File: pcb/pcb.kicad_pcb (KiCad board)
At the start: 2 copper layers, 70 x 21 mm, 20 parts, among them J1 BAT+, J2 BAT-, J3 Molex, SW1 Reset, SW2 Flash, U1 CP2102, U2 ESP-12F, U3 TP4056, U4 GY-521, U5 VREG

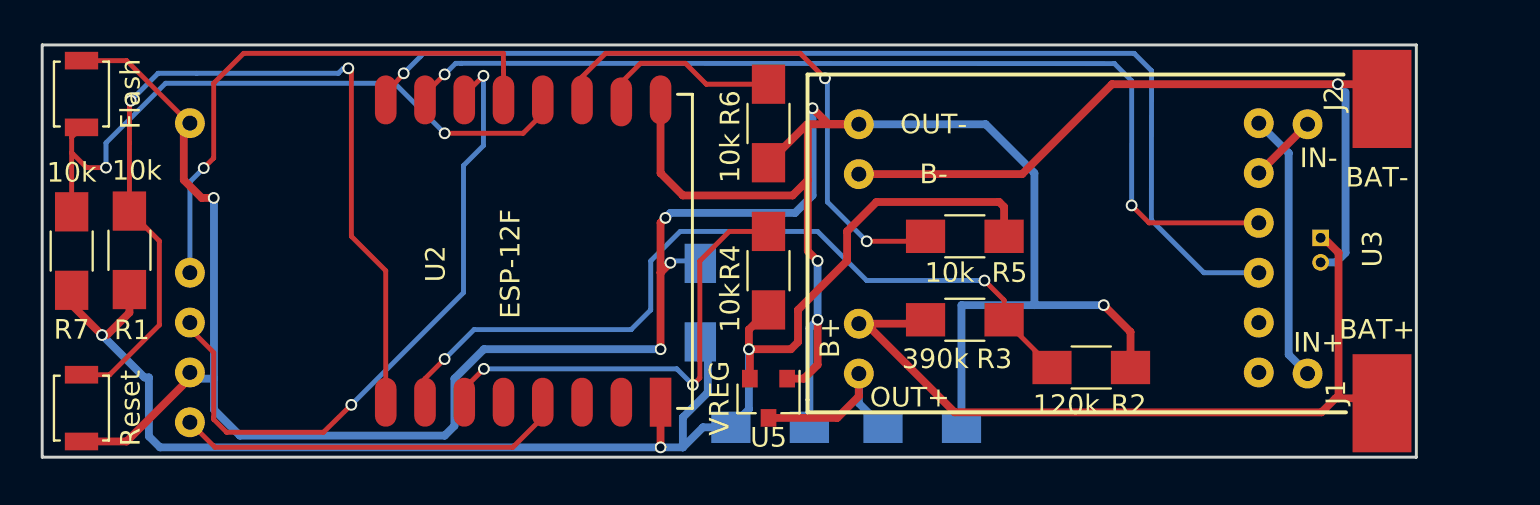
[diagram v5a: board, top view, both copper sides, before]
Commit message: Ignore BOM, remove old BOM, non-right-angle a few more traces
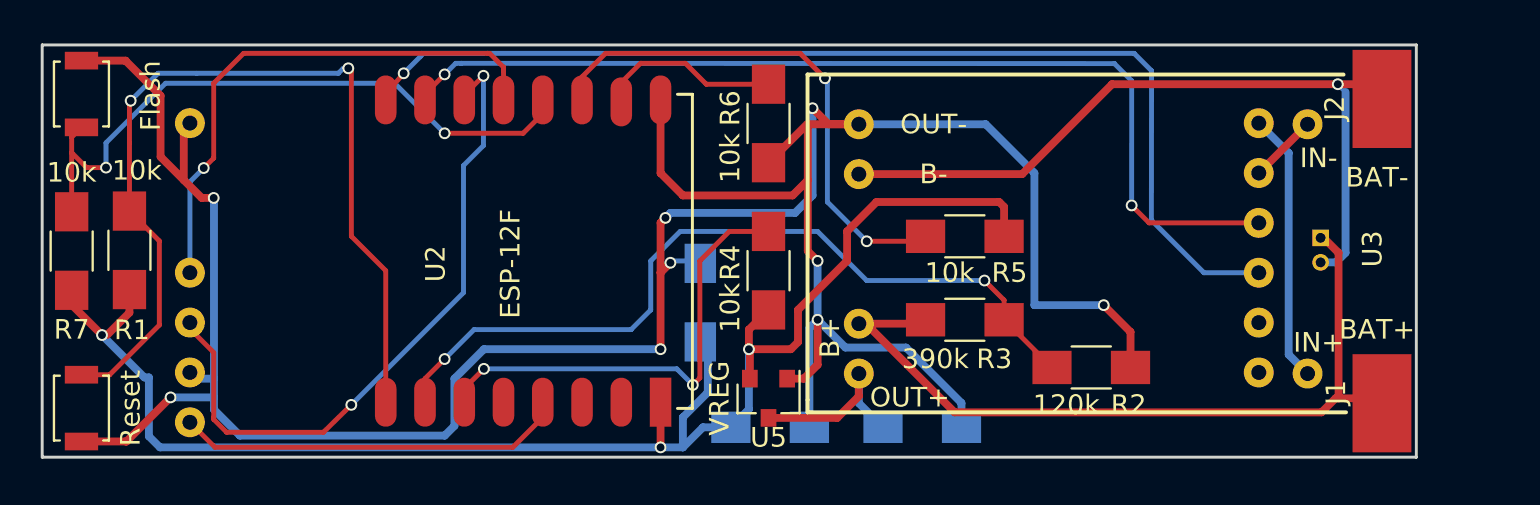
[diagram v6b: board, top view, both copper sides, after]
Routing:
- net /GND: track 152.5 -> 156.5 mm, vias 8 -> 9
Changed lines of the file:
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@@
     (area 106.162599 87.634999 176.312601 108.785001)
     (thickness 1.6)
-    (drawings 17)
-    (tracks 268)
+    (drawings 16)
+    (tracks 282)
     (zones 0)
     (modules 20)
@@
       (effects (font (size 1 1) (thickness 0.15)))
     )
-    (fp_text value Flash (at 0 2.5 90) (layer F.SilkS)
+    (fp_text value Flash (at -0.087 3.5224 90) (layer F.SilkS)
       (effects (font (size 1 1) (thickness 0.15)))
     )
@@
     (tags "MesurementPoint Square SMDPad 5mmx10mm ")
     (attr smd)
-    (fp_text reference J2 (at 0 -2.4384 90) (layer F.SilkS)
+    (fp_text reference J2 (at -0.472 -2.4026 90) (layer F.SilkS)
       (effects (font (size 1 1) (thickness 0.15)))
     )
@@
     (arrow2b (pts (xy 103.138 87.638) (xy 103.724421 88.764504)))
   )
-  (gr_line (start 128.23 87.778) (end 128.23 87.828) (angle 90) (layer B.Mask) (width 0.2))
-  (gr_line (start 128.23 108.678) (end 128.23 87.778) (angle 90) (layer B.Mask) (width 0.2))
-  (gr_line (start 112.23 87.778) (end 112.23 108.678) (angle 90) (layer B.Mask) (width 0.2))
+  (gr_line (start 128.23 108.678) (end 128.23 87.778) (angle 90) (layer B.SilkS) (width 0.2))
+  (gr_line (start 112.23 87.778) (end 112.23 108.678) (angle 90) (layer B.SilkS) (width 0.2))
   (gr_line (start 145.225 106.426) (end 172.657 106.426) (angle 90) (layer F.SilkS) (width 0.2))
   (gr_line (start 145.225 105.791) (end 145.225 106.426) (angle 90) (layer F.SilkS) (width 0.2))
@@
   (segment (start 130.2136 108.204) (end 115.0336 108.204) (width 0.25) (layer F.Cu) (net 10))
   (segment (start 131.7376 105.21) (end 131.7376 106.71) (width 0.25) (layer F.Cu) (net 10) (status 30))
-  (segment (start 116.4976 88.138) (end 129.731 88.138) (width 0.25) (layer F.Cu) (net 11))
+  (segment (start 128.905 88.138) (end 129.032 88.138) (width 0.25) (layer F.Cu) (net 11))
+  (segment (start 129.736189 88.842189) (end 129.736189 88.842132) (width 0.25) (layer F.Cu) (net 11))
+  (segment (start 129.032 88.138) (end 129.736189 88.842189) (width 0.25) (layer F.Cu) (net 11))
+  (segment (start 116.4976 88.138) (end 128.905 88.138) (width 0.25) (layer F.Cu) (net 11))
   (segment (start 129.7376 89.0336) (end 129.7376 91.21) (width 0.25) (layer F.Cu) (net 11) (status 20))
-  (segment (start 129.731 88.138) (end 129.7376 89.0336) (width 0.25) (layer F.Cu) (net 11))
+  (segment (start 129.736189 88.842132) (end 129.7376 89.0336) (width 0.25) (layer F.Cu) (net 11))
   (segment (start 113.7616 94.684) (end 114.4656 93.98) (width 0.25) (layer B.Cu) (net 11))
   (via (at 114.4656 93.98) (size 0.6) (drill 0.4) (layers F.Cu B.Cu) (net 11))
@@
   (segment (start 146.7376 106.71) (end 143.2376 106.71) (width 0.4) (layer F.Cu) (net 13) (status 20))
   (segment (start 147.8376 105.61) (end 146.7376 106.71) (width 0.4) (layer F.Cu) (net 13))
+  (segment (start 153.067 107.188) (end 153.067 105.95) (width 0.4) (layer B.Cu) (net 14) (status 400000))
+  (segment (start 147.1516 103.124) (end 145.7376 101.71) (width 0.4) (layer B.Cu) (net 14))
+  (segment (start 150.241 103.124) (end 147.1516 103.124) (width 0.4) (layer B.Cu) (net 14))
+  (segment (start 153.067 105.95) (end 150.241 103.124) (width 0.4) (layer B.Cu) (net 14))
+  (segment (start 110.5376 107.91) (end 110.5376 107.9024) (width 0.4) (layer F.Cu) (net 14))
+  (segment (start 108.2376 107.91) (end 110.49 107.91) (width 0.4) (layer F.Cu) (net 14) (status 20))
+  (segment (start 110.5376 107.91) (end 110.49 107.91) (width 0.4) (layer F.Cu) (net 14) (status 20))
+  (segment (start 112.776 105.664) (end 114.9876 105.664) (width 0.4) (layer B.Cu) (net 14))
+  (via (at 112.776 105.664) (size 0.6) (drill 0.4) (layers F.Cu B.Cu) (net 14))
+  (segment (start 110.5376 107.9024) (end 112.776 105.664) (width 0.4) (layer F.Cu) (net 14))
+  (segment (start 110.49 88.51) (end 110.49 88.519) (width 0.4) (layer F.Cu) (net 14))
+  (segment (start 112.268 93.408) (end 113.4496 94.5896) (width 0.4) (layer F.Cu) (net 14))
+  (segment (start 112.268 90.297) (end 112.268 93.408) (width 0.4) (layer F.Cu) (net 14))
+  (segment (start 110.49 88.519) (end 112.268 90.297) (width 0.4) (layer F.Cu) (net 14))
   (segment (start 156.782 100.965) (end 156.782 94.234) (width 0.4) (layer B.Cu) (net 14))
   (segment (start 154.298 91.75) (end 147.8376 91.75) (width 0.4) (layer B.Cu) (net 14))
@@
   (segment (start 144.463 95.377) (end 145.2376 94.6024) (width 0.4) (layer F.Cu) (net 14))
   (segment (start 137.7376 99.3084) (end 137.7376 103.21) (width 0.4) (layer F.Cu) (net 14))
-  (segment (start 114.9876 104.71) (end 114.9876 106.2876) (width 0.4) (layer B.Cu) (net 14))
+  (segment (start 114.9876 104.71) (end 114.9876 105.664) (width 0.4) (layer B.Cu) (net 14))
+  (segment (start 114.9876 105.664) (end 114.9876 106.2876) (width 0.4) (layer B.Cu) (net 14))
   (via (at 137.7376 103.21) (size 0.6) (drill 0.4) (layers F.Cu B.Cu) (net 14))
   (segment (start 137.7376 103.21) (end 128.7376 103.21) (width 0.4) (layer B.Cu) (net 14))
@@
   (segment (start 145.32 107.188) (end 145.32 102.1276) (width 0.4) (layer B.Cu) (net 14) (status 10))
   (segment (start 145.32 102.1276) (end 145.7376 101.71) (width 0.4) (layer B.Cu) (net 14))
-  (segment (start 153.067 107.188) (end 153.067 100.965) (width 0.4) (layer B.Cu) (net 14) (status 10))
   (segment (start 114.9876 95.518) (end 114.9736 95.504) (width 0.25) (layer B.Cu) (net 14))
   (via (at 114.9736 95.504) (size 0.6) (drill 0.4) (layers F.Cu B.Cu) (net 14))
@@
   (segment (start 161.6776 104.14) (end 161.6776 102.33) (width 0.4) (layer F.Cu) (net 14) (status 10))
   (segment (start 160.3126 100.965) (end 156.782 100.965) (width 0.4) (layer B.Cu) (net 14))
-  (segment (start 156.782 100.965) (end 153.067 100.965) (width 0.4) (layer B.Cu) (net 14))
   (via (at 160.3126 100.965) (size 0.6) (drill 0.4) (layers F.Cu B.Cu) (net 14))
   (segment (start 161.6776 102.33) (end 160.3126 100.965) (width 0.4) (layer F.Cu) (net 14))
   (segment (start 113.7616 91.692) (end 113.7196 91.692) (width 0.25) (layer F.Cu) (net 14) (status 30))
-  (segment (start 113.7196 91.692) (end 110.5376 88.51) (width 0.25) (layer F.Cu) (net 14) (status 10))
-  (segment (start 110.5376 88.51) (end 108.2376 88.51) (width 0.25) (layer F.Cu) (net 14) (status 20))
+  (segment (start 110.5376 88.51) (end 110.49 88.51) (width 0.25) (layer F.Cu) (net 14) (status 20))
+  (segment (start 110.49 88.51) (end 108.2376 88.51) (width 0.4) (layer F.Cu) (net 14) (status 20))
   (segment (start 113.7616 91.692) (end 113.7616 91.734) (width 0.25) (layer F.Cu) (net 14) (status 30))
   (segment (start 113.7616 104.392) (end 113.7616 104.686) (width 0.25) (layer F.Cu) (net 14) (status 30))
-  (segment (start 113.7616 104.686) (end 110.5376 107.91) (width 0.4) (layer F.Cu) (net 14) (status 10))
-  (segment (start 110.5376 107.91) (end 108.2376 107.91) (width 0.4) (layer F.Cu) (net 14) (status 20))
   (segment (start 114.9876 104.71) (end 114.0796 104.71) (width 0.4) (layer B.Cu) (net 14) (status 20))
   (segment (start 114.0796 104.71) (end 113.7616 104.392) (width 0.4) (layer B.Cu) (net 14) (status 30))

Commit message: Some significant design changes
Thanks to u/Triabolical_ and u/alez from r/PrintedCircuitBoards for their
feedback and advice.

1. Switch to 805 resistors and the non-hand-soldered PCB pad footprints
They're not appreciably harder to solder, given that they're only 0.01"
smaller than the 1206 size, and they make routing considerably easier.
The non-hand-soldered size will be a bit trickier, but not all that
much trickier.

2. Move components around
The ESP-12 antenna performs much better when it's open to air on all
sides. It's now at the top of the board, poking off the edge. The switches
and pullup/downs now live right below the ESP-12, the GY521 pins go below
them, and everything else is mostly the same. The ESP-12 smoothing capacitor
now lives directly between the VCC and ground pins.

The overall package is now 0.2mm longer, but the routing is cleaner and
fewer vias are required.
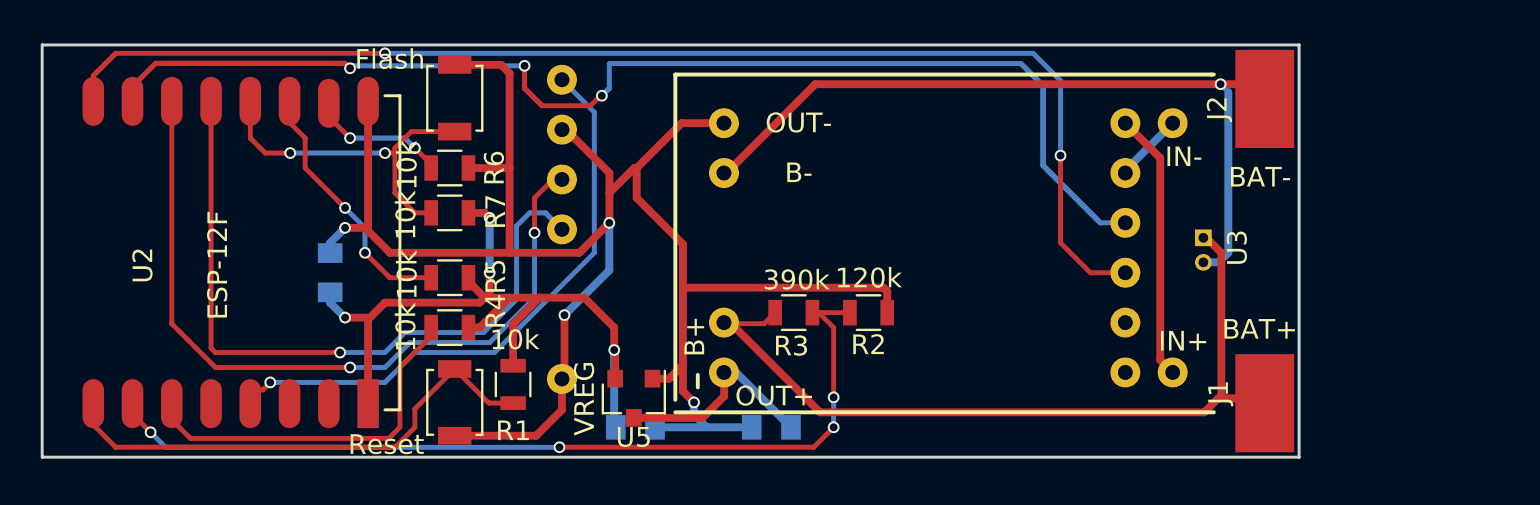
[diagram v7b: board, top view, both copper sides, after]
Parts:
- C1, C2, C3: footprint Capacitors_SMD:C_1206_HandSoldering -> Capacitors_SMD:C_0805
- R1, R2, R3, R4, R5, R6, R7: footprint Resistors_SMD:R_1206_HandSoldering -> Resistors_SMD:R_0805
- U1: value CP2102 -> CP2102-BREAKOUT
- moved U4 30.4 mm to (134.2, 87.7), turned to 180 degrees
- moved R5 26.3 mm to (127.0, 99.6)
- moved R1 20.7 mm to (130.2, 105.0), turned to 270 degrees
- moved R7 19.4 mm to (127.0, 96.3), turned to 180 degrees
- moved SW1 19.0 mm to (127.3, 105.9)
- moved SW2 19.0 mm to (127.3, 90.4)
- moved C1 18.9 mm to (120.9, 99.3)
- moved R4 16.5 mm to (127.0, 102.1), turned to 0 degrees
- moved R6 16.4 mm to (127.0, 94.0), turned to 180 degrees
- moved U2 14.9 mm to (108.8, 105.3)
- moved R2 11.7 mm to (148.3, 101.3)
- moved R3 8.72 mm to (144.5, 101.3)
- moved C2 7.69 mm to (143.4, 107.2), turned to 0 degrees
- moved U3 6.87 mm to (166.4, 89.2)
- moved C3 6.86 mm to (136.5, 107.2)
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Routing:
- net /GND: track 156.5 -> 99.0 mm, vias 9 -> 4
- net /3.3+: track 80.5 -> 40.0 mm, vias 3 -> 4
- net /HostTX: track 51.2 -> 85.8 mm, vias 2 -> 3
- net Net-(R1-Pad2): track 46.2 -> 26.6 mm, vias 2 -> 0
- net Net-(R7-Pad2): track 32.8 -> 16.8 mm
- net Net-(R5-Pad2): track 27.6 -> 12.5 mm
- net /HostRX: track 55.5 -> 66.1 mm, vias 1 -> 2
- net /GY+: track 22.1 -> 29.9 mm, vias 0 -> 1
- net /SDA: track 28.2 -> 35.5 mm
- net Net-(R2-Pad2): track 40.5 -> 46.5 mm, vias 2 -> 4
- net Net-(R6-Pad2): track 10.4 -> 6.49 mm, vias 0 -> 2
- net /SCL: track 35.2 -> 38.7 mm
- net Net-(R4-Pad1): track 23.0 -> 19.5 mm, vias 2 -> 0
- net /CHG+: track 9.46 -> 10.8 mm
- net Net-(J2-Pad1): track 39.1 -> 40.0 mm
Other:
- board size 70 x 21 mm -> 64 x 21 mm

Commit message: Add board name, version number, and OSHW logo
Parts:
- added G***: LOGO, OSHW:LOGO_5mm, B.Cu at (109.5, 94.5)
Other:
- board text added: "1.0.0-rc.1"
- board text added: "OSHW"
- board text added: "PendulumPCB"
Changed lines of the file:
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@@
     (area 99.863999 81.638 183.488 115.237992)
     (thickness 1.6)
-    (drawings 18)
+    (drawings 21)
     (tracks 255)
     (zones 0)
-    (modules 20)
+    (modules 21)
     (nets 19)
   )
@@
   )
   (setup
-    (last_trace_width 0.4)
+    (last_trace_width 0.25)
     (user_trace_width 0.4)
     (trace_clearance 0.2)
@@
     )
   )
+  (module OSHW:LOGO_5mm (layer B.Cu)
+    (at 109.538 94.538 90)
+    (fp_text reference G*** (at 0 -2.65176 90) (layer B.SilkS) hide
+      (effects (font (size 0.22606 0.22606) (thickness 0.04318)) (justify mirror))
+    )
+    (fp_text value LOGO (at 0 2.65176 90) (layer B.SilkS) hide
+      (effects (font (size 0.22606 0.22606) (thickness 0.04318)) (justify mirror))
+    )
+    (fp_poly (pts (xy -1.51384 -2.24536) (xy -1.48844 -2.23012) (xy -1.43002 -2.19456) (xy -1.3462 -2.13868)
+      (xy -1.24714 -2.07264) (xy -1.14808 -2.0066) (xy -1.0668 -1.95326) (xy -1.01092 -1.91516)
+      (xy -0.98552 -1.90246) (xy -0.97282 -1.90754) (xy -0.9271 -1.9304) (xy -0.85852 -1.96596)
+      (xy -0.81788 -1.98628) (xy -0.75692 -2.01168) (xy -0.7239 -2.0193) (xy -0.71882 -2.00914)
+      (xy -0.69596 -1.96088) (xy -0.6604 -1.8796) (xy -0.61468 -1.77038) (xy -0.5588 -1.64338)
+      (xy -0.50292 -1.50876) (xy -0.4445 -1.36906) (xy -0.38862 -1.23444) (xy -0.34036 -1.11506)
+      (xy -0.29972 -1.01854) (xy -0.27432 -0.94996) (xy -0.26416 -0.92202) (xy -0.2667 -0.9144)
+      (xy -0.29972 -0.88392) (xy -0.35306 -0.84328) (xy -0.47244 -0.74676) (xy -0.58928 -0.60198)
+      (xy -0.6604 -0.43688) (xy -0.68326 -0.25146) (xy -0.66294 -0.08128) (xy -0.5969 0.08128)
+      (xy -0.4826 0.2286) (xy -0.3429 0.33782) (xy -0.18034 0.4064) (xy 0 0.42926)
+      (xy 0.17272 0.40894) (xy 0.34036 0.3429) (xy 0.48768 0.23114) (xy 0.55118 0.16002)
+      (xy 0.63754 0.01016) (xy 0.6858 -0.14732) (xy 0.69088 -0.18796) (xy 0.68326 -0.36322)
+      (xy 0.63246 -0.5334) (xy 0.53848 -0.68326) (xy 0.40894 -0.80772) (xy 0.3937 -0.81788)
+      (xy 0.33528 -0.8636) (xy 0.29464 -0.89408) (xy 0.26416 -0.91948) (xy 0.48768 -1.45796)
+      (xy 0.52324 -1.54178) (xy 0.5842 -1.6891) (xy 0.63754 -1.8161) (xy 0.68072 -1.9177)
+      (xy 0.7112 -1.98374) (xy 0.7239 -2.01168) (xy 0.7239 -2.01422) (xy 0.74422 -2.01676)
+      (xy 0.78486 -2.00152) (xy 0.86106 -1.96596) (xy 0.90932 -1.94056) (xy 0.96774 -1.91262)
+      (xy 0.99314 -1.90246) (xy 1.016 -1.91516) (xy 1.06934 -1.95072) (xy 1.15062 -2.00406)
+      (xy 1.24714 -2.06756) (xy 1.33858 -2.13106) (xy 1.4224 -2.18694) (xy 1.48336 -2.22504)
+      (xy 1.51384 -2.24282) (xy 1.51892 -2.24282) (xy 1.54432 -2.22758) (xy 1.59258 -2.18694)
+      (xy 1.66624 -2.11836) (xy 1.77038 -2.01422) (xy 1.78562 -1.99898) (xy 1.87198 -1.91262)
+      (xy 1.94056 -1.83896) (xy 1.98628 -1.78816) (xy 2.00406 -1.7653) (xy 2.00406 -1.7653)
+      (xy 1.98882 -1.73482) (xy 1.95072 -1.67386) (xy 1.89484 -1.5875) (xy 1.82626 -1.48844)
+      (xy 1.64846 -1.22936) (xy 1.74498 -0.98552) (xy 1.77546 -0.90932) (xy 1.81356 -0.82042)
+      (xy 1.8415 -0.75438) (xy 1.85674 -0.72644) (xy 1.88214 -0.71628) (xy 1.95072 -0.70104)
+      (xy 2.04724 -0.68072) (xy 2.16154 -0.6604) (xy 2.2733 -0.64008) (xy 2.37236 -0.61976)
+      (xy 2.44348 -0.60706) (xy 2.4765 -0.59944) (xy 2.48412 -0.59436) (xy 2.49174 -0.57912)
+      (xy 2.49428 -0.5461) (xy 2.49682 -0.48514) (xy 2.49936 -0.39116) (xy 2.49936 -0.25146)
+      (xy 2.49936 -0.23622) (xy 2.49682 -0.10668) (xy 2.49428 0) (xy 2.49174 0.06604)
+      (xy 2.48666 0.09398) (xy 2.48666 0.09398) (xy 2.45618 0.1016) (xy 2.38506 0.11684)
+      (xy 2.286 0.13462) (xy 2.16662 0.15748) (xy 2.159 0.16002) (xy 2.04216 0.18288)
+      (xy 1.9431 0.2032) (xy 1.87198 0.21844) (xy 1.84404 0.2286) (xy 1.83642 0.23622)
+      (xy 1.81356 0.28194) (xy 1.78054 0.3556) (xy 1.7399 0.4445) (xy 1.7018 0.53848)
+      (xy 1.66878 0.6223) (xy 1.64592 0.68326) (xy 1.6383 0.7112) (xy 1.64084 0.71374)
+      (xy 1.65862 0.74168) (xy 1.69926 0.80264) (xy 1.75514 0.88646) (xy 1.82372 0.98806)
+      (xy 1.8288 0.99568) (xy 1.89738 1.09474) (xy 1.95326 1.1811) (xy 1.98882 1.23952)
+      (xy 2.00406 1.26746) (xy 2.00406 1.27) (xy 1.9812 1.30048) (xy 1.9304 1.35636)
+      (xy 1.85674 1.43256) (xy 1.77038 1.52146) (xy 1.74244 1.54686) (xy 1.64338 1.64338)
+      (xy 1.57734 1.70434) (xy 1.53416 1.73736) (xy 1.51384 1.74498) (xy 1.51384 1.74498)
+      (xy 1.48336 1.7272) (xy 1.41986 1.68656) (xy 1.33604 1.62814) (xy 1.23444 1.55956)
+      (xy 1.22682 1.55448) (xy 1.12776 1.4859) (xy 1.04394 1.43002) (xy 0.98552 1.38938)
+      (xy 0.95758 1.37414) (xy 0.95504 1.37414) (xy 0.9144 1.38684) (xy 0.84328 1.41224)
+      (xy 0.75438 1.44526) (xy 0.66294 1.48336) (xy 0.57912 1.51892) (xy 0.51562 1.54686)
+      (xy 0.48514 1.56464) (xy 0.48514 1.56464) (xy 0.47498 1.6002) (xy 0.4572 1.6764)
+      (xy 0.43688 1.778) (xy 0.41148 1.89992) (xy 0.40894 1.92024) (xy 0.38608 2.03962)
+      (xy 0.3683 2.13868) (xy 0.35306 2.20726) (xy 0.34544 2.2352) (xy 0.3302 2.23774)
+      (xy 0.27178 2.24282) (xy 0.18288 2.24536) (xy 0.07366 2.24536) (xy -0.0381 2.24536)
+      (xy -0.14732 2.24282) (xy -0.2413 2.24028) (xy -0.30988 2.2352) (xy -0.33782 2.23012)
+      (xy -0.33782 2.22758) (xy -0.34798 2.18948) (xy -0.36576 2.11582) (xy -0.38608 2.01168)
+      (xy -0.40894 1.88976) (xy -0.41402 1.8669) (xy -0.43688 1.75006) (xy -0.4572 1.651)
+      (xy -0.4699 1.58496) (xy -0.47752 1.55702) (xy -0.49022 1.55194) (xy -0.53848 1.53162)
+      (xy -0.61722 1.4986) (xy -0.71628 1.45796) (xy -0.94488 1.36652) (xy -1.22682 1.55702)
+      (xy -1.25222 1.5748) (xy -1.35382 1.64338) (xy -1.4351 1.69926) (xy -1.49352 1.73736)
+      (xy -1.51638 1.75006) (xy -1.51892 1.75006) (xy -1.54686 1.72466) (xy -1.60274 1.67132)
+      (xy -1.67894 1.59766) (xy -1.76784 1.5113) (xy -1.83134 1.44526) (xy -1.91008 1.36652)
+      (xy -1.95834 1.31318) (xy -1.98628 1.28016) (xy -1.9939 1.25984) (xy -1.99136 1.2446)
+      (xy -1.97358 1.21666) (xy -1.93294 1.1557) (xy -1.87452 1.06934) (xy -1.80594 0.97028)
+      (xy -1.75006 0.88646) (xy -1.6891 0.79248) (xy -1.651 0.72644) (xy -1.63576 0.69342)
+      (xy -1.64084 0.68072) (xy -1.65862 0.62484) (xy -1.69418 0.54102) (xy -1.73482 0.44196)
+      (xy -1.83388 0.22098) (xy -1.97866 0.19304) (xy -2.06756 0.17526) (xy -2.18948 0.1524)
+      (xy -2.30886 0.12954) (xy -2.49174 0.09398) (xy -2.49936 -0.58166) (xy -2.47142 -0.59436)
+      (xy -2.44348 -0.60198) (xy -2.3749 -0.61722) (xy -2.27838 -0.63754) (xy -2.16154 -0.65786)
+      (xy -2.06502 -0.67564) (xy -1.96596 -0.69596) (xy -1.89484 -0.70866) (xy -1.86436 -0.71628)
+      (xy -1.8542 -0.72644) (xy -1.83134 -0.7747) (xy -1.79578 -0.8509) (xy -1.75514 -0.94234)
+      (xy -1.71704 -1.03632) (xy -1.68148 -1.12522) (xy -1.65862 -1.19126) (xy -1.64846 -1.22428)
+      (xy -1.66116 -1.25222) (xy -1.69926 -1.31064) (xy -1.7526 -1.39192) (xy -1.82118 -1.49098)
+      (xy -1.88722 -1.5875) (xy -1.94564 -1.67132) (xy -1.98374 -1.73228) (xy -2.00152 -1.76022)
+      (xy -1.99136 -1.778) (xy -1.95326 -1.82626) (xy -1.8796 -1.90246) (xy -1.76784 -2.01168)
+      (xy -1.75006 -2.02946) (xy -1.6637 -2.11328) (xy -1.59004 -2.18186) (xy -1.5367 -2.22758)
+      (xy -1.51384 -2.24536)) (layer B.SilkS) (width 0.00254))
+  )
+  (gr_text 1.0.0-rc.1 (at 113.638 97.538 270) (layer B.SilkS)
+    (effects (font (size 1.5 1.5) (thickness 0.3)) (justify mirror))
+  )
+  (gr_text PendulumPCB (at 116.038 97.938 270) (layer B.SilkS)
+    (effects (font (size 1.5 1.5) (thickness 0.3)) (justify mirror))
+  )
+  (gr_text OSHW (at 109.238 100.538 270) (layer B.SilkS)
+    (effects (font (size 1.5 1.5) (thickness 0.3)) (justify mirror))
+  )
   (dimension 64.1 (width 0.3) (layer Dwgs.User)
